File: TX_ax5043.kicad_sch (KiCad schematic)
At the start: 30 parts, among them J7 2118714-2, P6 CONUFL001-SMD-T, P7 CONUFL001-SMD-T, Q7 DMP2065UQ, U23 AX5043

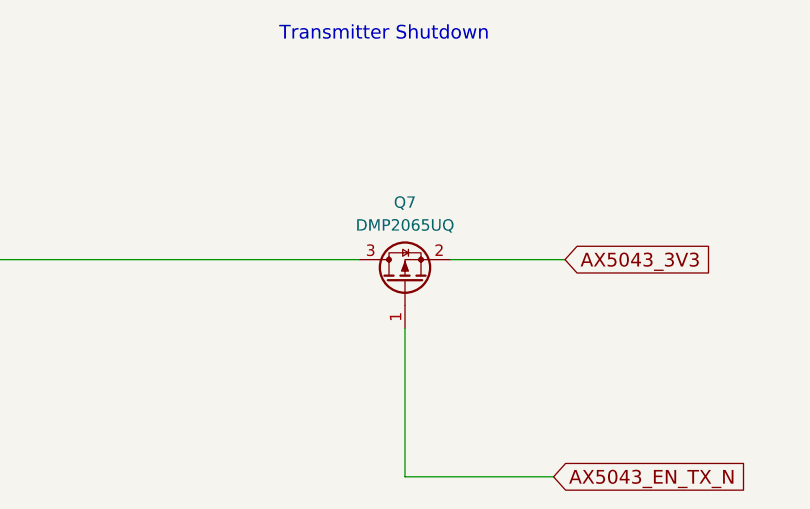
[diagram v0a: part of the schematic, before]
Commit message: Replace the AX5043 MOSFETs again
A little wider VTgs and lower on resistance.

Signed-off-by: Corey Minyard <corey@minyard.net>
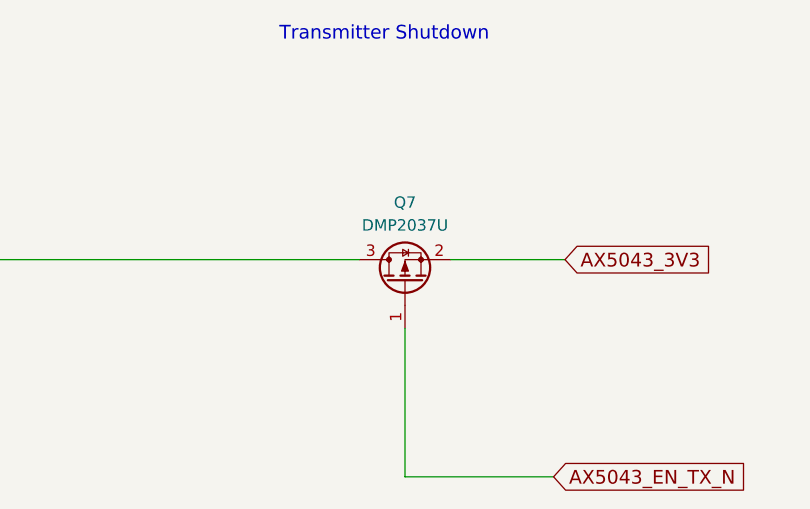
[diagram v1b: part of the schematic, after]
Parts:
- Q7: value DMP2065UQ -> DMP2037U
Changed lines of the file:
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@@
 			)
 		)
-		(property "Value" "DMP2065UQ"
+		(property "Value" "DMP2037U"
 			(at 342.9 77.47 90)
 			(effects

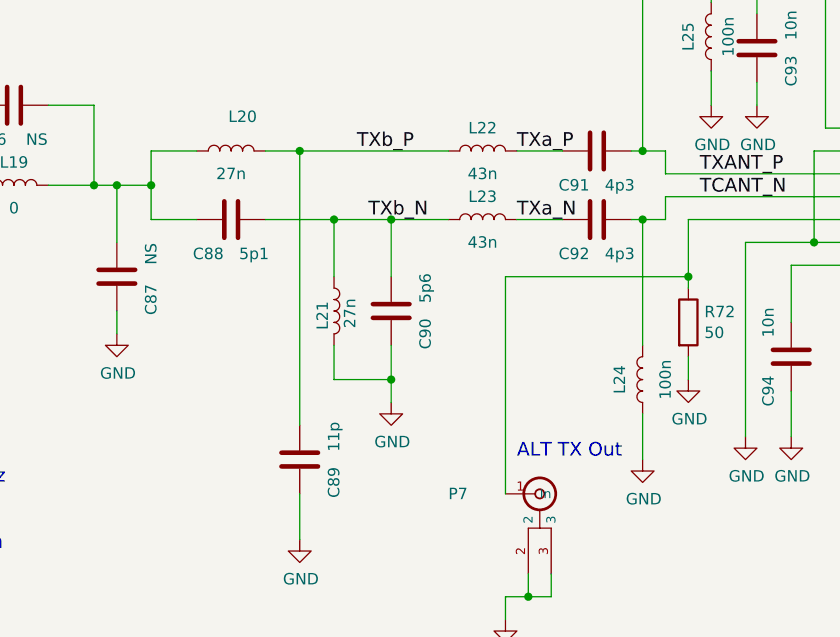
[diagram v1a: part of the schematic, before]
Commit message: Check over notes and some component values
Fix a wrong capacitor in one spot, set Q and voltage as necessary.

Signed-off-by: Corey Minyard <corey@minyard.net>
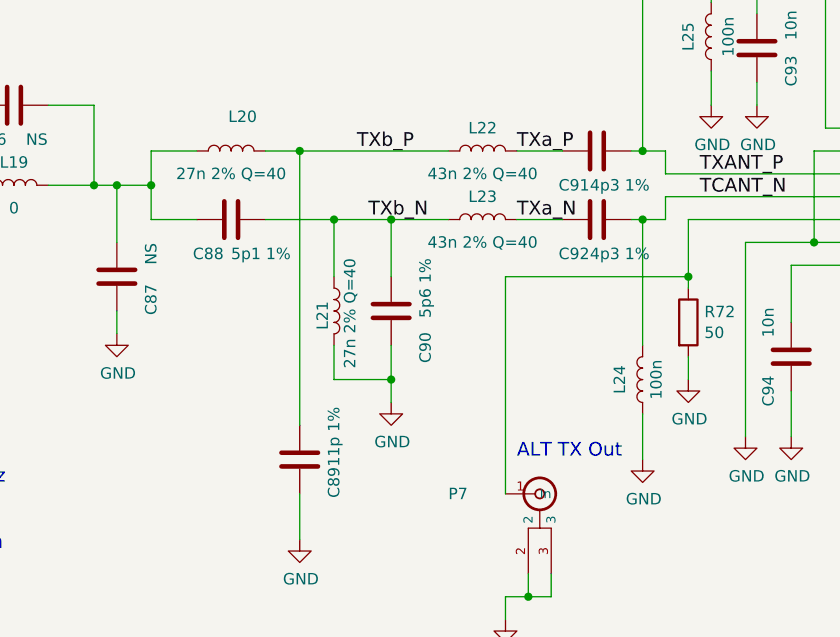
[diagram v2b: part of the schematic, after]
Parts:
- C88: value 5p1 -> 5p1 1%
- C89: value 11p -> 11p 1%
- C90: value 5p6 -> 5p6 1%
- C91, C92: value 4p3 -> 4p3 1%
- L20, L21: value 27n -> 27n 2% Q=40
- L22, L23: value 43n -> 43n 2% Q=40
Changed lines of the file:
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@@
 			)
 		)
-		(property "Value" "4p3"
+		(property "Value" "4p3 1%"
 			(at 215.9 135.89 90)
 			(effects
@@
 			)
 		)
-		(property "Value" "4p3"
+		(property "Value" "4p3 1%"
 			(at 215.9 143.51 90)
 			(effects
@@
 		(dnp no)
 		(property "Reference" "C90"
-			(at 194.31 152.4 90)
-			(effects
-				(font
-					(size 1.27 1.27)
-				)
-			)
-		)
-		(property "Value" "5p6"
+			(at 194.31 153.924 90)
+			(effects
+				(font
+					(size 1.27 1.27)
+				)
+			)
+		)
+		(property "Value" "5p6 1%"
 			(at 194.31 147.32 90)
 			(effects
@@
 			)
 		)
-		(property "Value" "27n"
+		(property "Value" "27n 2% Q=40"
 			(at 185.928 150.114 90)
 			(effects
@@
 			)
 		)
-		(property "Value" "5p1"
-			(at 175.26 143.51 90)
+		(property "Value" "5p1 1%"
+			(at 176.022 143.51 90)
 			(effects
 				(font
@@
 			)
 		)
-		(property "Value" "11p"
+		(property "Value" "11p 1%"
 			(at 184.15 163.83 90)
 			(effects
@@
 			)
 		)
-		(property "Value" "43n"
+		(property "Value" "43n 2% Q=40"
 			(at 200.66 142.24 90)
 			(effects
@@
 			)
 		)
-		(property "Value" "43n"
+		(property "Value" "43n 2% Q=40"
 			(at 200.66 134.62 90)
 			(effects
@@
 		)
 		(property "Value" "100n"
-			(at 220.98 157.48 90)
+			(at 219.964 157.48 90)
 			(effects
 				(font
@@
 			)
 		)
-		(property "Value" "27n"
+		(property "Value" "27n 2% Q=40"
 			(at 172.72 134.62 90)
 			(effects

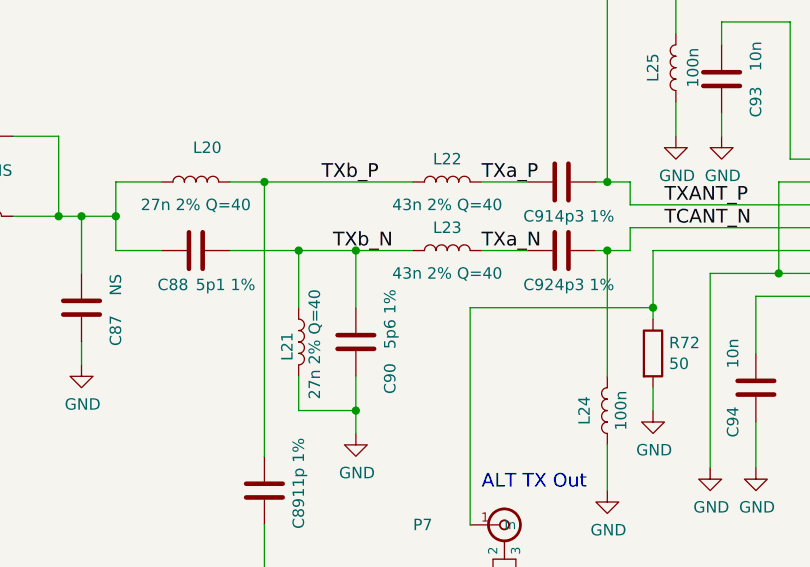
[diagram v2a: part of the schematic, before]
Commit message: Fix values of a lot of parts
Make them standard, 4.1p instead of 4p1, etc.

Add a tag to a couple of ICs that didn't have a pin 1 indicator on the
board.

Signed-off-by: Corey Minyard <corey@minyard.net>
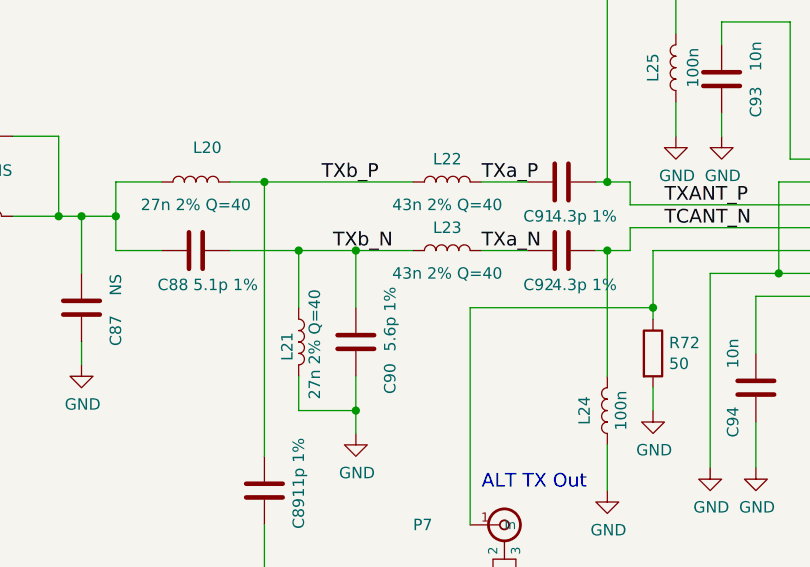
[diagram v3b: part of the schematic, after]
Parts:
- C88: value 5p1 1% -> 5.1p 1%
- C90: value 5p6 1% -> 5.6p 1%
- C91, C92: value 4p3 1% -> 4.3p 1%
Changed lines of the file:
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@@
 			)
 		)
-		(property "Value" "4p3 1%"
+		(property "Value" "4.3p 1%"
 			(at 215.9 135.89 90)
 			(effects
@@
 			)
 		)
-		(property "Value" "4p3 1%"
+		(property "Value" "4.3p 1%"
 			(at 215.9 143.51 90)
 			(effects
@@
 			)
 		)
-		(property "Value" "5p6 1%"
+		(property "Value" "5.6p 1%"
 			(at 194.31 147.32 90)
 			(effects
@@
 			)
 		)
-		(property "Value" "5p1 1%"
+		(property "Value" "5.1p 1%"
 			(at 176.022 143.51 90)
 			(effects

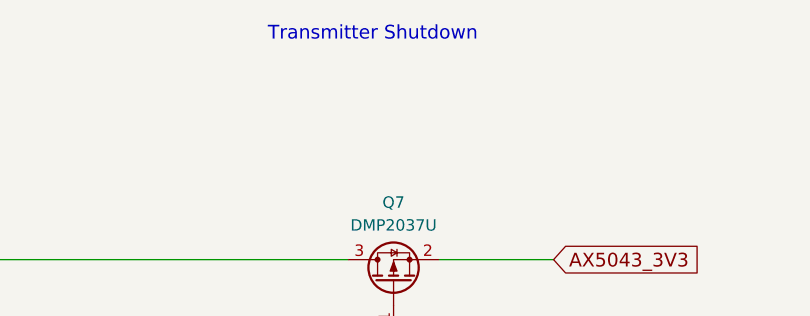
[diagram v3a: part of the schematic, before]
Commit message: Add some notes, fix the diode footprints on the RTC
Signed-off-by: Corey Minyard <corey@minyard.net>
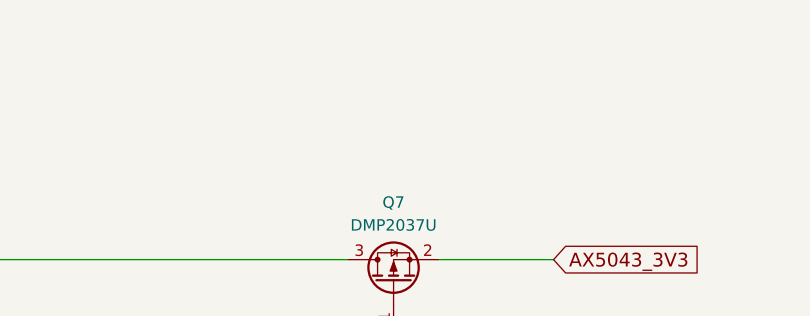
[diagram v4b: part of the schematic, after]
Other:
- note removed: "Transmitter Shutdown"
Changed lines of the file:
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@@
 		(comment 1 "N5BRG")
-	)
-	(text "Transmitter Shutdown"
-		(exclude_from_sim no)
-		(at 328.93 57.15 0)
-		(effects
-			(font
-				(size 1.524 1.524)
-			)
-			(justify left bottom)
-		)
 	)
 	(text "TX_DRV"

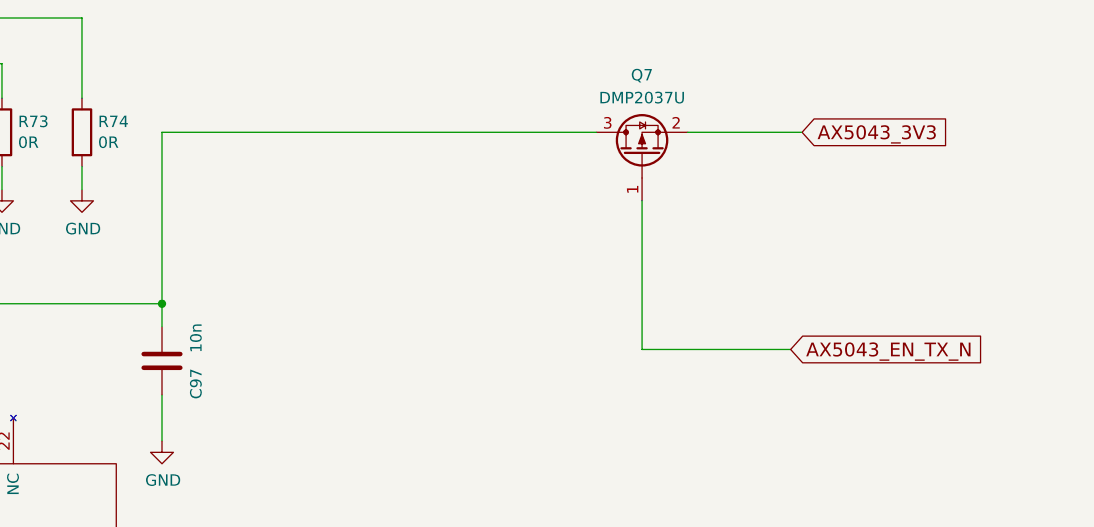
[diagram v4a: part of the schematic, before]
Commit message: Add ferrite beads to the AX5043s' power inputs
Signed-off-by: Corey Minyard <corey@minyard.net>
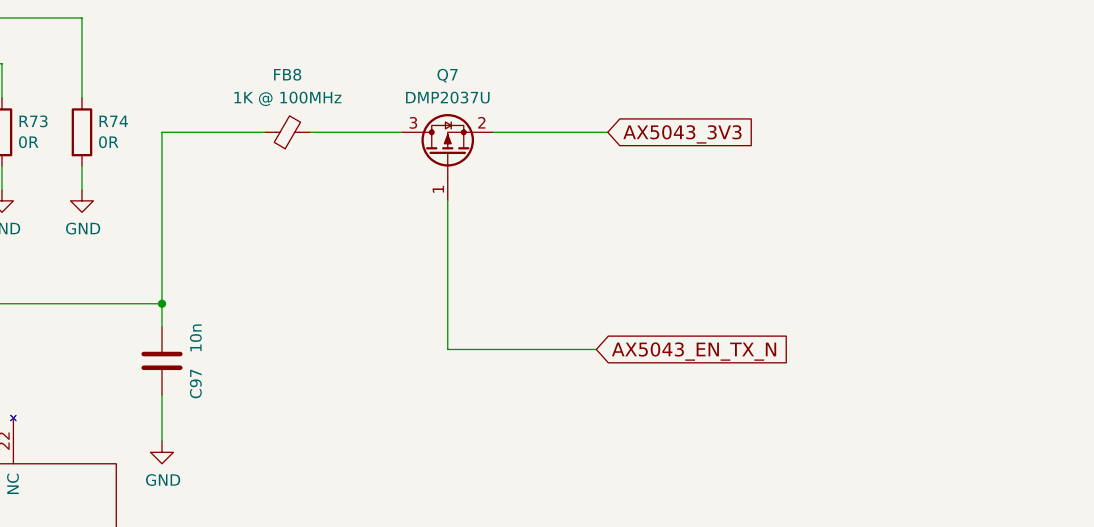
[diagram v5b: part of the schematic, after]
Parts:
- added FB8: 1K @ 100MHz, Resistor_SMD:R_0603_1608Metric_Pad0.98x0.95mm_HandSolder, symbol Device:FerriteBead_Small
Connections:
- net at C97.1, U23.23 (VDD_IO): now also FB8.1; no longer Q7.3 (D)
- new net: FB8.2, Q7.3 (D)
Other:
- moved on the sheet: Q7
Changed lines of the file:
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@@
 	(wire
 		(pts
-			(xy 347.98 81.28) (xy 360.68 81.28)
+			(xy 326.39 81.28) (xy 339.09 81.28)
 		)
 		(stroke
@@
 	(wire
 		(pts
+			(xy 306.07 81.28) (xy 316.23 81.28)
+		)
+		(stroke
+			(width 0)
+			(type default)
+		)
+	)
+	(wire
+		(pts
 			(xy 160.02 149.86) (xy 160.02 152.4)
 		)
@@
 	(wire
 		(pts
-			(xy 289.56 81.28) (xy 337.82 81.28)
+			(xy 289.56 81.28) (xy 300.99 81.28)
 		)
 		(stroke
@@
 	(wire
 		(pts
-			(xy 342.9 88.9) (xy 342.9 105.41)
+			(xy 321.31 88.9) (xy 321.31 105.41)
 		)
 		(stroke
@@
 	(wire
 		(pts
-			(xy 342.9 105.41) (xy 359.41 105.41)
+			(xy 321.31 105.41) (xy 337.82 105.41)
 		)
 		(stroke
@@
 	(global_label "AX5043_3V3"
 		(shape input)
-		(at 360.68 81.28 0)
+		(at 339.09 81.28 0)
 		(fields_autoplaced yes)
 		(effects
@@
 		)
 		(property "Intersheetrefs" "${INTERSHEET_REFS}"
-			(at 377.3149 81.28 0)
+			(at 355.7249 81.28 0)
 			(effects
 				(font
@@
 	(global_label "AX5043_EN_TX_N"
 		(shape input)
-		(at 359.41 105.41 0)
+		(at 337.82 105.41 0)
 		(fields_autoplaced yes)
 		(effects
@@
 		)
 		(property "Intersheetrefs" "${INTERSHEET_REFS}"
-			(at 381.438 105.41 0)
+			(at 359.848 105.41 0)
 			(effects
 				(font
@@
 	)
 	(symbol
+		(lib_id "Device:FerriteBead_Small")
+		(at 303.53 81.28 90)
+		(unit 1)
+		(exclude_from_sim no)
+		(in_bom yes)
+		(on_board yes)
+		(dnp no)
+		(fields_autoplaced yes)
+		(property "Reference" "FB8"
+			(at 303.4919 74.93 90)
+			(effects
+				(font
+					(size 1.27 1.27)
+				)
+			)
+		)
+		(property "Value" "1K @ 100MHz"
+			(at 303.4919 77.47 90)
+			(effects
+				(font
+					(size 1.27 1.27)
+				)
+			)
+		)
+		(property "Footprint" "Resistor_SMD:R_0603_1608Metric_Pad0.98x0.95mm_HandSolder"
+			(at 303.53 83.058 90)
+			(effects
+				(font
+					(size 1.27 1.27)
+				)
+				(hide yes)
+			)
+		)
+		(property "Datasheet" "~"
+			(at 303.53 81.28 0)
+			(effects
+				(font
+					(size 1.27 1.27)
+				)
+				(hide yes)
+			)
+		)
+		(property "Description" "FerriteBead_Small"
+			(at 303.53 81.28 0)
+			(effects
+				(font
+					(size 1.27 1.27)
+				)
+				(hide yes)
+			)
+		)
+		(pin "1"
+		)
+		(pin "2"
+		)
+		(instances
+			(project "PacSat_AFSK"
+				(path "/cc9f42d2-6985-41ac-acab-5ab7b01c5b38/d9a83ee4-3280-49b9-88b8-54d26cbd8ed1/2fc9a4ba-520e-46cf-be0c-1f13bbb64152"
+					(reference "FB8")
+					(unit 1)
+				)
+			)
+		)
+	)
+	(symbol
 		(lib_id "power:GND")
 		(at 275.59 163.83 0)
@@
 	(symbol
 		(lib_id "Transistor_FET:Q_PMOS_GSD")
-		(at 342.9 83.82 90)
+		(at 321.31 83.82 90)
 		(unit 1)
 		(exclude_from_sim no)
@@
 		(fields_autoplaced yes)
 		(property "Reference" "Q7"
-			(at 342.9 74.93 90)
+			(at 321.31 74.93 90)
 			(effects
 				(font
@@
 		)
 		(property "Value" "DMP2037U"
-			(at 342.9 77.47 90)
+			(at 321.31 77.47 90)
 			(effects
 				(font
@@
 		)
 		(property "Footprint" "Package_TO_SOT_SMD:SOT-23"
-			(at 340.36 78.74 0)
+			(at 318.77 78.74 0)
 			(effects
 				(font
@@
 		)
 		(property "Datasheet" "~"
-			(at 342.9 83.82 0)
+			(at 321.31 83.82 0)
 			(effects
 				(font
@@
 		)
 		(property "Description" "P-MOSFET transistor, gate/source/drain"
-			(at 342.9 83.82 0)
+			(at 321.31 83.82 0)
 			(effects
 				(font
